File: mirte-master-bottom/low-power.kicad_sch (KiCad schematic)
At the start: 9 parts, among them J12 USB_A, J19 5V, J2 5vConverter, J21 3V3, U10 DB125-2.54-2P-GN

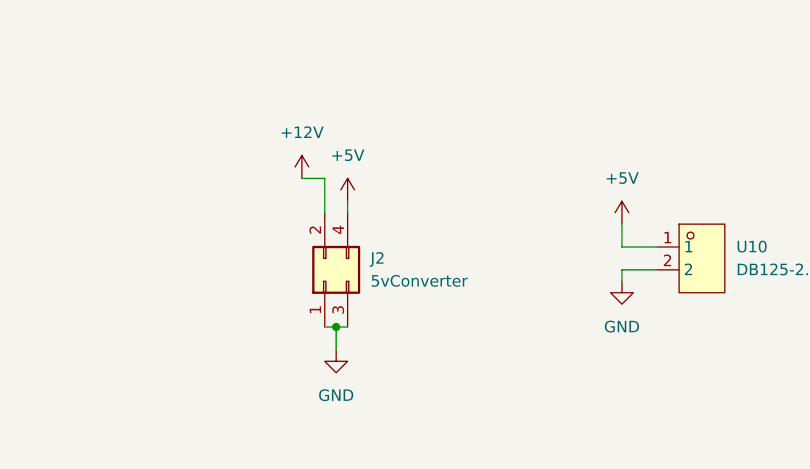
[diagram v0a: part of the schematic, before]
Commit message: MM: ERC&DRC fixes + change hbridge cap
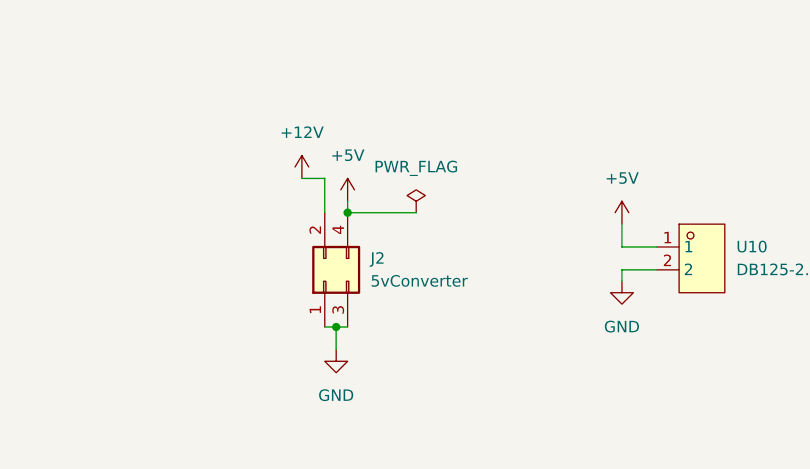
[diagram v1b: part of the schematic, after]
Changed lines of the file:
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@@
+	)
+	(junction
+		(at 137.16 144.78)
+		(diameter 0)
+		(color 0 0 0 0)
 	)
 	(junction
@@
 	(wire
 		(pts
+			(xy 137.16 144.78) (xy 144.78 144.78)
+		)
+		(stroke
+			(width 0)
+			(type default)
+		)
+	)
+	(wire
+		(pts
 			(xy 67.31 147.32) (xy 67.31 149.86)
 		)
@@
 		)
 	)
+	(symbol
+		(lib_id "power:PWR_FLAG")
+		(at 144.78 144.78 0)
+		(unit 1)
+		(exclude_from_sim no)
+		(in_bom yes)
+		(on_board yes)
+		(dnp no)
+		(fields_autoplaced yes)
+		(property "Reference" "#FLG02"
+			(at 144.78 142.875 0)
+			(effects
+				(font
+					(size 1.27 1.27)
+				)
+				(hide yes)
+			)
+		)
+		(property "Value" "PWR_FLAG"
+			(at 144.78 139.7 0)
+			(effects
+				(font
+					(size 1.27 1.27)
+				)
+			)
+		)
+		(property "Footprint" ""
+			(at 144.78 144.78 0)
+			(effects
+				(font
+					(size 1.27 1.27)
+				)
+				(hide yes)
+			)
+		)
+		(property "Datasheet" "~"
+			(at 144.78 144.78 0)
+			(effects
+				(font
+					(size 1.27 1.27)
+				)
+				(hide yes)
+			)
+		)
+		(property "Description" "Special symbol for telling ERC where power comes from"
+			(at 144.78 144.78 0)
+			(effects
+				(font
+					(size 1.27 1.27)
+				)
+				(hide yes)
+			)
+		)
+		(pin "1"
+		)
+		(instances
+			(project "mirte-master-bottom"
+				(path "/c479422a-501d-4123-8665-56a1c70bd9ea/2572bf06-cf54-4115-a4c7-ccf0e044675d/b99b3764-9ce2-4390-a177-5fc4973f5d88"
+					(reference "#FLG02")
+					(unit 1)
+				)
+			)
+		)
+	)

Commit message: MM: order big
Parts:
- U10: LCSC (none) -> C918120
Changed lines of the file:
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@@
+			)
+		)
+		(property "LCSC" "C918120"
+			(at 180.34 148.5899 0)
+			(effects
+				(font
+					(size 1.27 1.27)
+				)
+				(hide yes)
 			)
 		)
